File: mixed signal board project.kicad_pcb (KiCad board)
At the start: 4 copper layers, 70 x 70 mm, 190 parts, among them J101 USB_B_Mini, J102 Conn_01x06_Pin, J201 8P8C_Shielded, J301 Conn_01x04_Pin, J401 AudioJack3, J402 Conn_01x04_Pin, J403 Screw_Terminal_01x03, J501 USB_B_Mini, J701 Conn_01x02_Socket, J801 Conn_01x02_Socket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

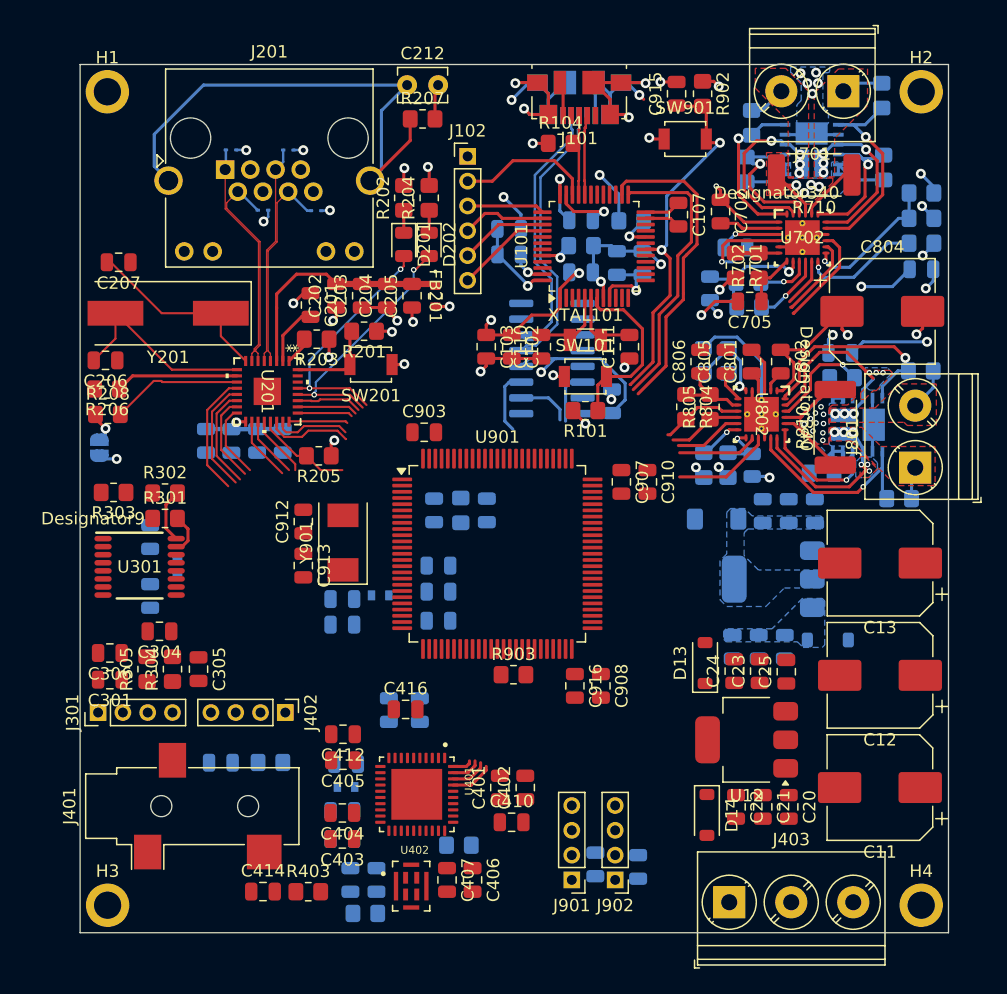
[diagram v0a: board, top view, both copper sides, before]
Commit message: MIC footprint changed, all blocks routed internally, next step is route all to the MCU
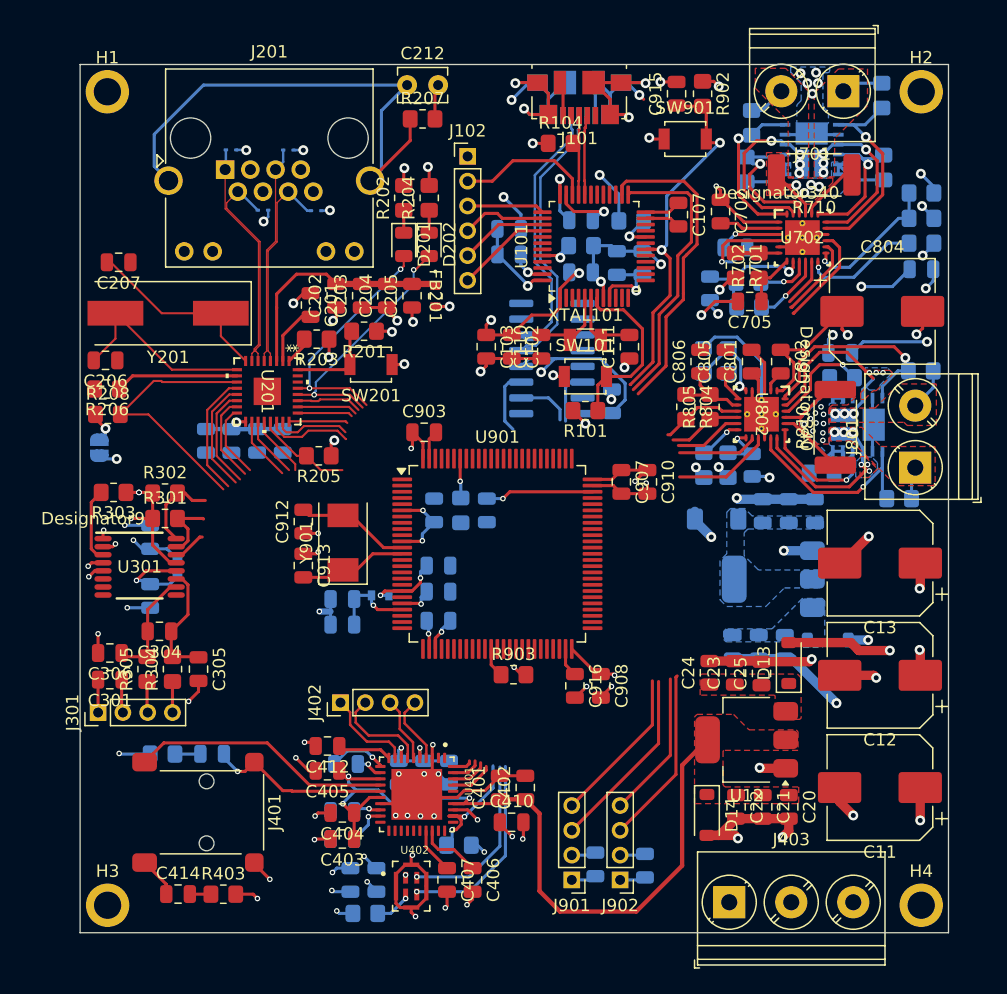
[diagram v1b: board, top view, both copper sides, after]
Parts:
- C416: moved to B.Cu
- J401: footprint Connector_Audio:Jack_3.5mm_CUI_SJ-3523-SMT_Horizontal -> Connector_Audio:Jack_3.5mm_Lumberg_1503_02_Horizontal
- moved R402 8.73 mm to (76.7, 109.0), turned to 180 degrees
- moved R403 6.85 mm to (81.6, 120.3)
- moved C414 6.85 mm to (78.0, 120.3)
- moved D13 6.75 mm to (127.2, 101.7)
- moved C416 6.19 mm to (99.8, 110.5), turned to -90 degrees
- moved FB401 6.00 mm to (97.3, 113.0)
- moved C415 5.80 mm to (97.8, 110.5), turned to -90 degrees
- moved C417 5.33 mm to (95.8, 110.5), turned to -90 degrees
- moved J402 4.52 mm to (91.0, 104.9), turned to 90 degrees
- moved C23 2.00 mm to (122.8, 102.5)
- moved C24 2.00 mm to (120.8, 102.5)
- moved C25 2.00 mm to (125.0, 102.5)
- moved C412 1.57 mm to (90.0, 108.4)
- moved C405 1.51 mm to (90.0, 110.4)
- moved J401 1.44 mm to (77.8, 113.8)
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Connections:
- J901 pad 3: /STM32F407/EXT_UART_TX -> /STM32F407/EXT_UART_RX
- J901 pad 4: /STM32F407/EXT_UART_RX -> /STM32F407/EXT_UART_TX
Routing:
- net GND: track 149.5 -> 294.5 mm, vias 39 -> 88
- net +3V3: track 69.2 -> 140.6 mm, vias 15 -> 37
- net +1V8: track 0.00 -> 43.6 mm, vias 0 -> 1
- net Net-(U401-HP/LINE_OUTB): track 0.00 -> 24.3 mm
- net /DAC adn MIC/VA: track 0.00 -> 18.2 mm, vias 0 -> 2
- net +12V: track 37.5 -> 54.3 mm, vias 11 -> 16
- net /DAC adn MIC/CLK_MIC: track 0.00 -> 15.8 mm, vias 0 -> 1
- net /STM32F407/EXT_UART_RX: track 0.00 -> 14.9 mm
- net Net-(U401-HP/LINE_OUTA): track 0.00 -> 14.7 mm, vias 0 -> 1
- net /STM32F407/CAN_TX: track 0.00 -> 14.4 mm
- net /DAC adn MIC/DOUT_MIC: track 0.00 -> 14.2 mm, vias 0 -> 1
- net /STM32F407/EXT_UART_TX: track 0.00 -> 12.7 mm
- net /STM32F407/CAN_RX: track 0.00 -> 11.9 mm
- net /Ethernet/ETH_MDIO: track 10.6 -> 21.4 mm
- net /DAC adn MIC/~{RESET}_DAC: track 0.00 -> 10.1 mm, vias 0 -> 2
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- added copper zone on F.Cu, net +1V8
- added copper zone on F.Cu, net Net-(D13-K)

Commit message: some design failures reviewed(MIC VDD is 1V8, Motor Drivers' pull-up to DVDD pin, I2C net fixed). Routing mostly done.
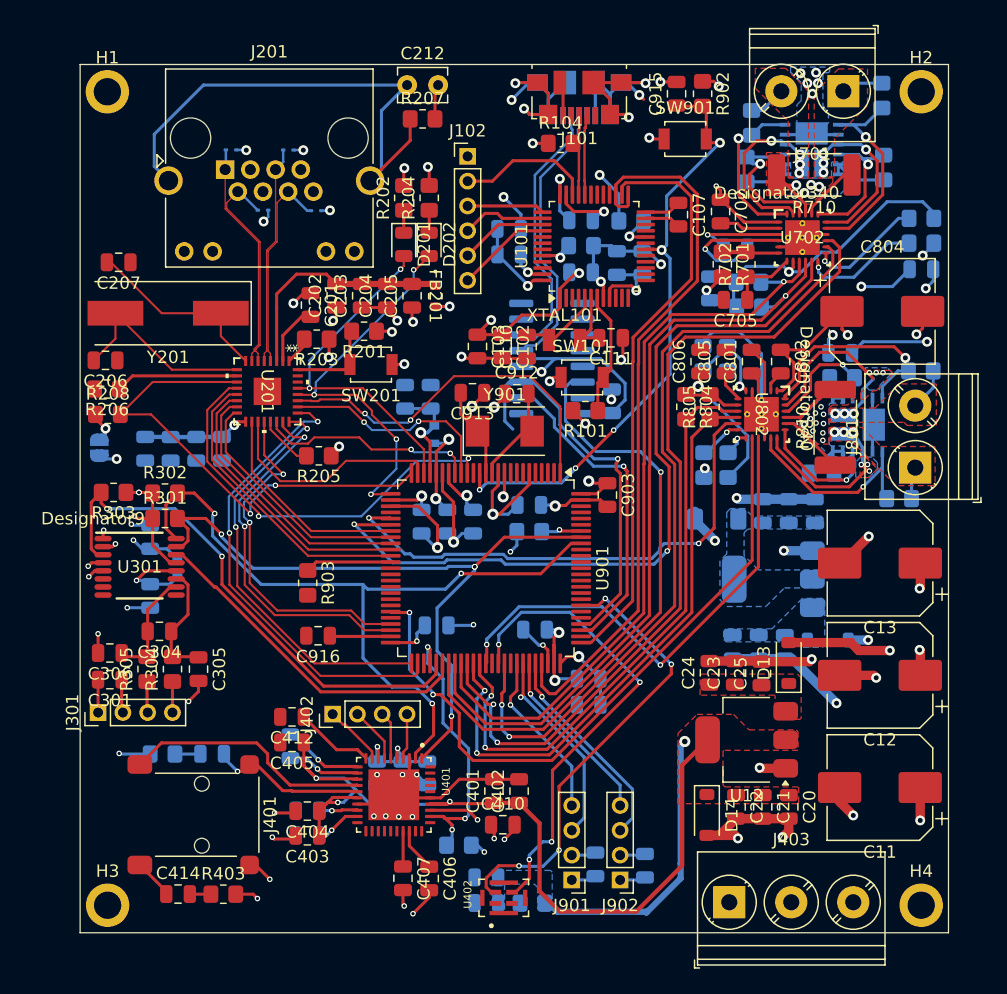
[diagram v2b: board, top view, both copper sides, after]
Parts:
- removed R711: 7k2, Resistor_SMD:R_0805_2012Metric_Pad1.20x1.40mm_HandSolder
- removed R812: 3k3, Resistor_SMD:R_0805_2012Metric
- C907, C908, C910: moved to B.Cu
- R710, R810: value 50m -> 50M
- R712: value 3k3 -> 100k
- R811: value 7k2 -> 100k
- moved C916 21.1 mm to (89.2, 99.5), turned to 180 degrees
- moved C912 20.1 mm to (105.3, 80.0), turned to 0 degrees
- moved C913 19.5 mm to (101.7, 79.9), turned to 180 degrees
- moved C902 19.1 mm to (96.3, 80.2), turned to 90 degrees
- moved R903 18.2 mm to (88.4, 95.2), turned to -90 degrees
- moved C907 18.2 mm to (111.1, 105.1), turned to 180 degrees
- moved C901 17.8 mm to (98.3, 80.2), turned to 90 degrees
- moved C910 16.6 mm to (111.1, 103.0), turned to 180 degrees
- moved Y901 15.8 mm to (104.3, 83.0), turned to 0 degrees
- moved C903 15.6 mm to (112.6, 88.2), turned to -90 degrees
- moved C908 14.1 mm to (98.8, 98.7), turned to 0 degrees
- moved FB901 13.7 mm to (98.6, 83.3), turned to -90 degrees
- moved R404 13.5 mm to (106.5, 121.1), turned to 0 degrees
- moved C419 11.0 mm to (102.8, 119.0), turned to 180 degrees
- moved C917 10.4 mm to (106.7, 99.0), turned to 0 degrees
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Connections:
- C418 pad 1: +3V3 -> +1V8
- C419 pad 1: +3V3 -> +1V8
- R301 pad 2: /ADC/SDA_ADC -> /ADC/SDA
- R302 pad 2: /ADC/SCK_ADC -> /ADC/SCL
- R404 pad 2: +3V3 -> +1V8
- R712 pad 2: GND -> DVDD_2
- R811 pad 2: +12V -> DVDD_1
- U301 pad 15: /ADC/SDA_ADC -> /ADC/SDA
- U301 pad 16: /ADC/SCK_ADC -> /ADC/SCL
- U401 pad 1: /DAC adn MIC/SDA_DAC -> /ADC/SDA
- U401 pad 2: /DAC adn MIC/SCL_DAC -> /ADC/SCL
- U402 pad 1: +3V3 -> +1V8
- U901 pad 92: /DAC adn MIC/SCL_DAC -> /ADC/SCL
- U901 pad 93: /DAC adn MIC/SDA_DAC -> /ADC/SDA
- U901 pad 95: /ADC/SCK_ADC -> unconnected-(U901-PB8-Pad95)
- U901 pad 96: /ADC/SDA_ADC -> unconnected-(U901-PB9-Pad96)
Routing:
- net /ADC/SCL: track 0.00 -> 61.1 mm, vias 0 -> 3
- net /Motor_Driver2/PH_2: track 8.21 -> 67.9 mm, vias 0 -> 2
- net /Motor_Driver2/SO_2: track 4.00 -> 63.4 mm, vias 0 -> 2
- net /Motor_Driver2/SNSOUT_2: track 5.79 -> 63.0 mm
- net /ADC/SDA: track 0.00 -> 56.9 mm, vias 0 -> 4
- net /Motor_Driver2/EN_2: track 6.64 -> 63.4 mm, vias 0 -> 2
- net /Motor_Driver2/nFAULT_2: track 4.42 -> 60.8 mm
- net /Motor_Driver1/EN: track 6.45 -> 55.0 mm, vias 0 -> 2
- net /STM32F407/CH340_~{RST}: track 4.29 -> 49.7 mm, vias 0 -> 1
- net /Motor_Driver1/SNSOUT: track 5.98 -> 48.5 mm, vias 0 -> 2
- net /Motor_Driver1/nFAULT: track 6.69 -> 48.5 mm, vias 0 -> 2
- net /Debugger/JTMS_F407: track 22.8 -> 59.9 mm
- net /ADC/RESET_ADC: track 6.03 -> 42.6 mm, vias 0 -> 2
- net /Motor_Driver1/SO: track 5.53 -> 42.1 mm, vias 0 -> 2
- net /Ethernet/ETH_TX_D1: track 4.45 -> 37.8 mm, vias 0 -> 2
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- added copper zone on B.Cu, net +1V8

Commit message: all tracks routed, ERC checked, silkscreens reviewed. Next step is PDN Analysis
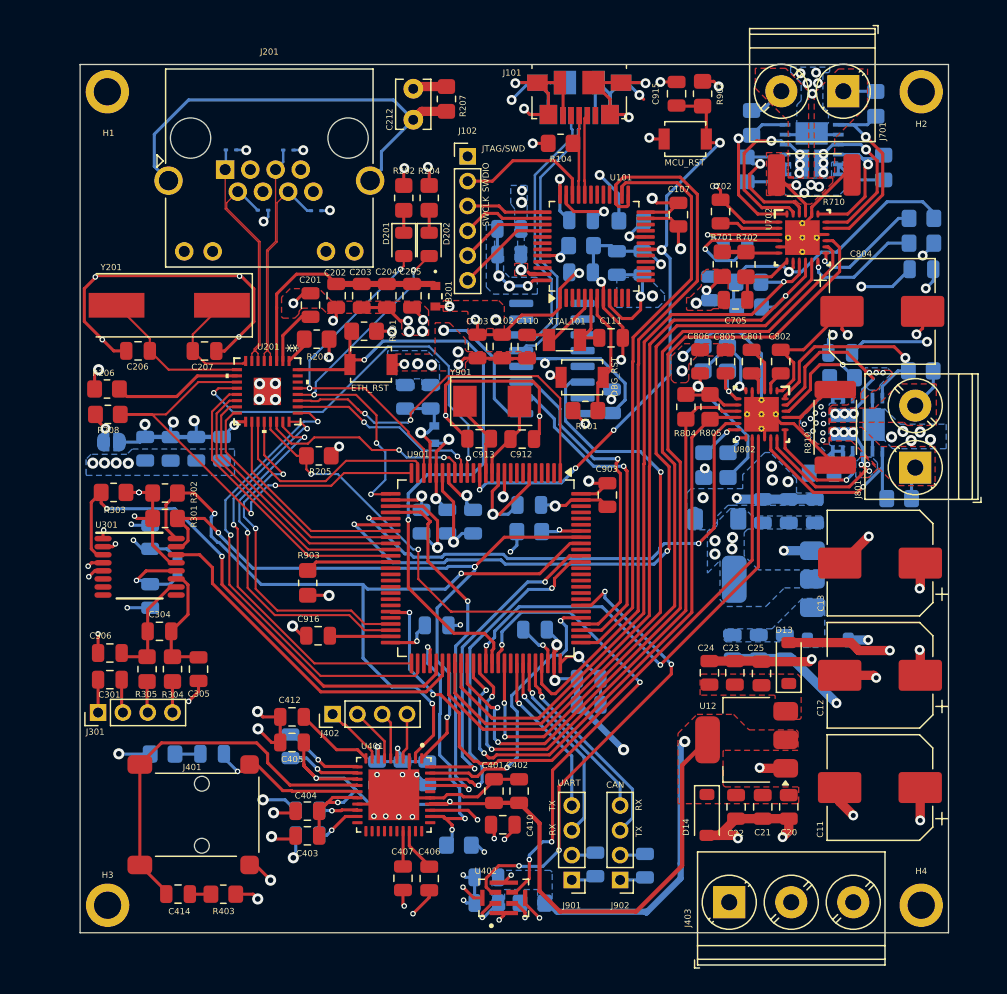
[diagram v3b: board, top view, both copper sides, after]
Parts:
- moved C207 9.96 mm to (80.1, 76.5)
- moved C913 3.74 mm to (102.2, 83.6), turned to 0 degrees
- moved C912 3.69 mm to (105.7, 83.6), turned to 180 degrees
- moved C212 2.84 mm to (96.9, 57.9), turned to 90 degrees
- moved C206 2.73 mm to (74.7, 76.5), turned to 0 degrees
- moved Y901 2.62 mm to (103.3, 80.6)
- moved R207 2.51 mm to (99.6, 56.2), turned to 90 degrees
- moved JP201 1.07 mm to (72.6, 83.9), turned to 0 degrees
- moved R703 0.82 mm to (134.2, 56.6)
- moved Y201 0.65 mm to (77.2, 72.9)
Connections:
- H1 pad 1: (no net) -> Earth
- H4 pad 1: (no net) -> Earth_2
- J403 pad 2: GNDPWR -> +12V
- J403 pad 3: +12V -> Earth_2
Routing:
- net GND: track 289.2 -> 383.3 mm, vias 79 -> 119
- net /Ethernet/RESET_PHY: track 7.13 -> 52.8 mm, vias 0 -> 2
- net /DAC adn MIC/MCLK_DAC: track 0.00 -> 30.7 mm, vias 0 -> 2
- net /Ethernet/ETH_INT: track 4.40 -> 33.8 mm, vias 0 -> 2
- net /DAC adn MIC/SCLK_DAC: track 0.00 -> 27.9 mm, vias 0 -> 2
- net /DAC adn MIC/LRCK_DAC: track 0.00 -> 26.6 mm, vias 0 -> 2
- net /DAC adn MIC/SDIN_DAC: track 0.00 -> 23.2 mm, vias 0 -> 2
- net +3V3: track 157.9 -> 167.0 mm, vias 32 -> 43
- net Net-(U401-HP/LINE_OUTB): track 23.3 -> 31.4 mm
- net /Ethernet/ETH_XO: track 15.6 -> 9.43 mm
- net /Ethernet/RJ_45_SH: track 41.5 -> 36.2 mm
- net /STM32F407/CH340_RXD: track 31.5 -> 26.7 mm
- net /Ethernet/ETH_XI: track 16.2 -> 12.4 mm
- net +1V8: track 68.6 -> 72.1 mm, vias 2 -> 3
- net Net-(U402-LR): track 0.00 -> 3.09 mm, vias 0 -> 1
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- added copper zone on F.Cu, net +3V3
- added copper zone on In2.Cu, net Earth
- added copper zone on In2.Cu, net Earth_2
- added copper zone on B.Cu, net GND
- added copper zone on F.Cu, net GND
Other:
- board text added: "CAN"
- board text added: "DBG_RST"
- board text added: "ETH_RST"
- board text added: "JTAG/SWD"
- board text added: "JTCK"
- board text added: "JTDI"
- board text added: "JTDO"
- board text added: "JTMS"
- board text added: "MCU_RST"
- board text added: "NJTRST"
- board text added: "RX"
- board text added: "SWCLK"
- board text added: "SWDIO"
- board text added: "TX"
- board text added: "UART"

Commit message: some additions
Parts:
- added REF**: KiCad-Logo2_6mm_SilkScreen, Symbol:KiCad-Logo2_6mm_SilkScreen, F.Cu at (120.5, 92.8)
- added REF**: OSHW-Logo2_14.6x12mm_SilkScreen, Symbol:OSHW-Logo2_14.6x12mm_SilkScreen, B.Cu at (127.2, 111.5)
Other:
- board text added: "Complete Electronics Hardware Design Course Project"
- board text added: "V2.0"

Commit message: updates
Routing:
- net /DAC adn MIC/LRCK_DAC: track 26.6 -> 25.4 mm
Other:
- board text added: "+12V"
- board text added: "+3V3"
- board text added: "12V"
- board text added: "EARTH"
- board text added: "GND"
